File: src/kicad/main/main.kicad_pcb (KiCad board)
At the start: 2 copper layers, 38 x 75 mm, 58 parts

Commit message: Use latest faebryk features
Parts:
- removed *.mcu_pcb.co2_sensor.decoupling_caps[0][Capacitor:C], *.mcu_pcb.co2_sensor.decoupling_caps[1][Capacitor:C], *.mcu_pcb.ldo.decoupling_caps[0][Capacitor:C], *.mcu_pcb.ldo.decoupling_caps[1][Capacitor:C], *.mcu_pcb.leds.buffer.decoupling_cap[Capacitor:C], *.mcu_pcb.leds.leds[0].decoupling_cap[Capacitor:C], *.mcu_pcb.leds.leds[1].decoupling_cap[Capacitor:C], *.mcu_pcb.leds.leds[2].decoupling_cap[Capacitor:C], *.mcu_pcb.leds.leds[3].decoupling_cap[Capacitor:C], *.mcu_pcb.leds.leds[4].decoupling_cap[Capacitor:C], *.mcu_pcb.lux_sensor.decoupling_cap[Capacitor:C], *.mcu_pcb.lux_sensor.dvi_capacitor[Capacitor:C], *.mcu_pcb.mcu.debounce_capacitors[0][Capacitor:C], *.mcu_pcb.mcu.debounce_capacitors[1][Capacitor:C], *.mcu_pcb.mcu.en_rc_capacitor[Capacitor:C], *.mcu_pcb.mcu.pwr_3v3_decoupling_caps[0][Capacitor:C], *.mcu_pcb.pm_sensor.pm_sensor_buffer.buffer.decouple_caps[0][Capacitor:C], *.mcu_pcb.pm_sensor.pm_sensor_buffer.buffer.decouple_caps[1][Capacitor:C], *.mcu_pcb.usb_psu.esd_capacitor[Capacitor:C], *.mcu_pcb.usb_psu.gnd_capacitor[Capacitor:C]: C, lcsc:C0402
- removed *.mcu_pcb.co2_sensor.pullup_resistors[0][Resistor:b'10.0k\xce\xa9'], *.mcu_pcb.co2_sensor.pullup_resistors[1][Resistor:b'10.0k\xce\xa9'], *.mcu_pcb.lux_sensor.i2c_termination_resistors[0][Resistor:b'10.0k\xce\xa9'], *.mcu_pcb.lux_sensor.i2c_termination_resistors[1][Resistor:b'10.0k\xce\xa9'], *.mcu_pcb.mcu.boot_resistors[0][Resistor:b'10.0k\xce\xa9'], *.mcu_pcb.mcu.boot_resistors[1][Resistor:b'10.0k\xce\xa9'], *.mcu_pcb.mcu.debounce_resistors[0][Resistor:b'10.0k\xce\xa9'], *.mcu_pcb.mcu.debounce_resistors[1][Resistor:b'10.0k\xce\xa9'], *.mcu_pcb.mcu.en_rc_resesitor[Resistor:b'10.0k\xce\xa9']: b'10.0k\xce\xa9', lcsc:R0402
- removed *.mcu_pcb.co2_sensor.scd4x[SCD40:U]: U, lcsc:LGA-20_L10.1-W10.1-P1.25-TL
- removed *.mcu_pcb.ldo[ME6211C33M5G_N:U]: U, lcsc:SOT-23-5_L3.0-W1.7-P0.95-LS2.8-BL
- removed *.mcu_pcb.leds.buffer.buffer[pf_74AHCT2G125:U]: U, lcsc:SC-74A-5_L2.9-W1.6-P0.95-LS2.8-BR
- removed *.mcu_pcb.leds.leds[0].led[XL_3528RGBW_WS2812B:LED], *.mcu_pcb.leds.leds[1].led[XL_3528RGBW_WS2812B:LED], *.mcu_pcb.leds.leds[2].led[XL_3528RGBW_WS2812B:LED], *.mcu_pcb.leds.leds[3].led[XL_3528RGBW_WS2812B:LED], *.mcu_pcb.leds.leds[4].led[XL_3528RGBW_WS2812B:LED]: LED, lcsc:LED-SMD_4P-L3.5-W2.8-BR-1
- removed *.mcu_pcb.lux_sensor.dvi_resistor[Resistor:b'1.0k\xce\xa9'], *.mcu_pcb.pm_sensor.fan_controller.led.current_limiting_resistor[Resistor:b'1.0k\xce\xa9']: b'1.0k\xce\xa9', lcsc:R0402
- removed *.mcu_pcb.lux_sensor[BH1750FVI_TR:U]: U, lcsc:WSOF-6_L2.6-W1.6-P0.50-TL-EP
- removed *.mcu_pcb.mcu.pwr_3v3_decoupling_caps[1][Capacitor:C]: C, lcsc:C0805
- removed *.mcu_pcb.mcu.switches[0][_Switch:SW], *.mcu_pcb.mcu.switches[1][_Switch:SW]: SW, lcsc:KEY-SMD_4P-L4.2-W3.2-P2.20-LS4.6
- removed *.mcu_pcb.mcu[ESP32_C3_MINI_1_VIND:U]: U, lcsc:WIFIM-SMD_ESP32-C3-MINI-MINI-1U
- removed *.mcu_pcb.pm_sensor.fan_connector.plug[pf_533984002:J]: J, lcsc:CONN-SMD_1.25-2P
- removed *.mcu_pcb.pm_sensor.fan_controller.fan_power_switch.mosfet[MOSFET:Q]: Q, lcsc:SOT-23-3_L2.9-W1.3-P1.90-LS2.4-BR
- removed *.mcu_pcb.pm_sensor.fan_controller.fan_power_switch.pull_resistor[Resistor:b'100.0k\xce\xa9']: b'100.0k\xce\xa9', lcsc:R0402
- removed *.mcu_pcb.pm_sensor.fan_controller.flyback_protection_diode[Diode:40V]: 40V, lcsc:SOD-323_L1.8-W1.3-LS2.5-RD
- removed *.mcu_pcb.pm_sensor.fan_controller.led.led[LED:D]: D, lcsc:LED0805-RD_RED
- removed *.mcu_pcb.pm_sensor.pm_sensor_buffer.buffer[TXS0102DCUR:U]: U, lcsc:VSON8_L2.0-W2.3-P0.50-LS3.1-BL
- removed *.mcu_pcb.pm_sensor.pm_sensor_connector.plug[B4B_ZR_SM4_TF:J]: J, lcsc:CONN-SMD_ZH1.5-4AB
- removed *.mcu_pcb.pressence_sensor[HLK_LD2410B_P:U]: U, lcsc:SENSORM-TH_HLK-LD2410B-P
- removed *.mcu_pcb.qwiic_connector[QWIIC:J]: J, lcsc:CONN-SMD_BM04B-SRSS-TBT-LF-SN
- removed *.mcu_pcb.usb_psu.configuration_resistors[0][Resistor:b'5.1k\xce\xa9'], *.mcu_pcb.usb_psu.configuration_resistors[1][Resistor:b'5.1k\xce\xa9']: b'5.1k\xce\xa9', lcsc:R0402
- removed *.mcu_pcb.usb_psu.esd[USBLC6_2P6:U]: U, lcsc:SOT-666-6_L1.6-W1.2-P0.50-LS1.6-BL
- removed *.mcu_pcb.usb_psu.gnd_resistor[Resistor:b'1.0M\xce\xa9']: b'1.0M\xce\xa9', lcsc:R0402
- removed *.mcu_pcb.usb_psu.usb_connector[USB_Type_C_Receptacle_14_pin_Vertical:x]: x, lcsc:USB-C-TH_TYPE-C-USB-14P
- added C1: 100nF, lcsc:C0402, F.Cu at (1.15, 5.00)
- added C10: 100nF, lcsc:C0402, B.Cu at (0.00, 37.9)
- added C11: 100nF, lcsc:C0402, B.Cu at (0.00, 5.25)
- added C12: 1µF, lcsc:C0402, B.Cu at (-1.25, 8.75)
- added C13: 100nF, lcsc:C0402, F.Cu at (10.8, 60.0)
- added C14: 100nF, lcsc:C0402, F.Cu at (-10.8, 60.0)
- added C15: 1µF, lcsc:C0402, F.Cu at (-7.90, 22.5)
- added C16: 100nF, lcsc:C0402, F.Cu at (-15.0, 23.8)
- added C17: 10µF, lcsc:C0805, F.Cu at (-14.8, 22.0)
- added C18: 100nF, lcsc:C0402, F.Cu at (-3.00, 2.50)
- added C19: 100nF, lcsc:C0402, F.Cu at (3.00, 2.50)
- added C2: 4.7µF, lcsc:C0402, F.Cu at (1.15, 18.0)
- added C20: 1µF, lcsc:C0402, F.Cu at (-7.50, 63.5)
- added C21: 100nF, lcsc:C0402, F.Cu at (-5.50, 73.0)
- added C3: 1µF, lcsc:C0402, F.Cu at (3.00, 66.0)
- added C4: 1µF, lcsc:C0402, F.Cu at (-3.00, 66.0)
- added C5: 100nF, lcsc:C0402, F.Cu at (-1.50, 30.0)
- added C6: 100nF, lcsc:C0402, B.Cu at (0.00, 13.5)
- added C7: 100nF, lcsc:C0402, B.Cu at (0.00, 19.6)
- added C8: 100nF, lcsc:C0402, B.Cu at (0.00, 25.7)
- added C9: 100nF, lcsc:C0402, B.Cu at (0.00, 31.8)
- added D1: LED, lcsc:LED0805-RD_RED, F.Cu at (8.00, 27.5)
- added H1: Mounting_Hole, MountingHole:MountingHole_2.1mm, F.Cu at (-6.50, 2.50)
- added H2: Mounting_Hole, MountingHole:MountingHole_2.1mm, F.Cu at (7.50, 69.5)
- added H3: Mounting_Hole, MountingHole:MountingHole_2.1mm, F.Cu at (-7.50, 69.5)
- added J1: pf_533984002, lcsc:CONN-SMD_1.25-2P, F.Cu at (2.00, 23.0)
- added J2: B4B_ZR_SM4_TF, lcsc:CONN-SMD_ZH1.5-4AB, F.Cu at (13.0, 21.0)
- added J3: QWIIC, lcsc:CONN-SMD_BM04B-SRSS-TBT-LF-SN, F.Cu at (16.0, 12.5)
- added LED1: XL_3528RGBW_WS2812B, lcsc:LED-SMD_4P-L3.5-W2.8-BR-1, B.Cu at (0.00, 11.0)
- added LED2: XL_3528RGBW_WS2812B, lcsc:LED-SMD_4P-L3.5-W2.8-BR-1, B.Cu at (0.00, 17.1)
- added LED3: XL_3528RGBW_WS2812B, lcsc:LED-SMD_4P-L3.5-W2.8-BR-1, B.Cu at (0.00, 23.2)
- added LED4: XL_3528RGBW_WS2812B, lcsc:LED-SMD_4P-L3.5-W2.8-BR-1, B.Cu at (0.00, 29.3)
- added LED5: XL_3528RGBW_WS2812B, lcsc:LED-SMD_4P-L3.5-W2.8-BR-1, B.Cu at (0.00, 35.4)
- added Q1: MOSFET, lcsc:SOT-23-3_L2.9-W1.3-P1.90-LS2.4-BR, F.Cu at (2.50, 27.5)
- added R1: 10kΩ, lcsc:R0402, F.Cu at (4.25, 18.5)
- added R10: 10kΩ, lcsc:R0402, F.Cu at (-9.40, 22.5)
- added R11: 100kΩ, lcsc:R0402, F.Cu at (2.50, 30.0)
- added R12: 1kΩ, lcsc:R0402, F.Cu at (8.00, 30.5)
- added R13: 390Ω, lcsc:R0402, F.Cu at (5.00, 1.75)
- added R14: 390Ω, lcsc:R0402, F.Cu at (5.00, 3.00)
- added R15: 5.1kΩ, lcsc:R0402, F.Cu at (2.50, 68.5)
- added R16: 5.1kΩ, lcsc:R0402, F.Cu at (-2.50, 68.5)
- added R17: 1MΩ, lcsc:R0402, F.Cu at (5.50, 73.0)
- added R2: 10kΩ, lcsc:R0402, F.Cu at (5.50, 18.5)
- added R3: 1kΩ, lcsc:R0402, B.Cu at (1.25, 8.75)
- added R4: 10kΩ, lcsc:R0402, B.Cu at (-12.2, 12.0)
- added R5: 10kΩ, lcsc:R0402, B.Cu at (-12.2, 13.2)
- added R6: 10kΩ, lcsc:R0402, F.Cu at (-4.25, 10.2)
- added R7: 10kΩ, lcsc:R0402, F.Cu at (-11.8, 22.5)
- added R8: 10kΩ, lcsc:R0402, F.Cu at (10.8, 63.0)
- added R9: 10kΩ, lcsc:R0402, F.Cu at (-10.8, 63.0)
- added SW1: _Switch, lcsc:KEY-SMD_4P-L4.2-W3.2-P2.20-LS4.6, F.Cu at (13.5, 61.5)
- added SW2: _Switch, lcsc:KEY-SMD_4P-L4.2-W3.2-P2.20-LS4.6, F.Cu at (-13.5, 61.5)
- added U1: SCD40, lcsc:LGA-20_L10.1-W10.1-P1.25-TL, F.Cu at (3.00, 11.5)
- added U2: ME6211C33M5G_N, lcsc:SOT-23-5_L3.0-W1.7-P0.95-LS2.8-BL, F.Cu at (0.00, 66.0)
- added U3: pf_74AHCT2G125, lcsc:SC-74A-5_L2.9-W1.6-P0.95-LS2.8-BR, F.Cu at (-1.50, 27.5)
- added U4: BH1750FVI_TR, lcsc:WSOF-6_L2.6-W1.6-P0.50-TL-EP, B.Cu at (0.00, 7.00)
- added U5: ESP32_C3_MINI_1_VIND, lcsc:WIFIM-SMD_ESP32-C3-MINI-MINI-1U, F.Cu at (-11.0, 13.0)
- added U6: TXS0102DCUR, lcsc:VSON8_L2.0-W2.3-P0.50-LS3.1-BL, F.Cu at (0.00, 2.50)
- added U7: HLK_LD2410B_P, lcsc:SENSORM-TH_HLK-LD2410B-P, B.Cu at (16.2, 61.5)
- added U8: USBLC6_2P6, lcsc:SOT-666-6_L1.6-W1.2-P0.50-LS1.6-BL, F.Cu at (-5.00, 64.5)
- added x1: USB_Type_C_Receptacle_14_pin_Vertical, lcsc:USB-C-TH_TYPE-C-USB-14P, F.Cu at (0.00, 73.2)
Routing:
- added copper zone on B.Cu, net GND
- added copper zone on F.Cu, net GND
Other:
- outline, holes or cut-outs redrawn
- copper layers 2 -> 4

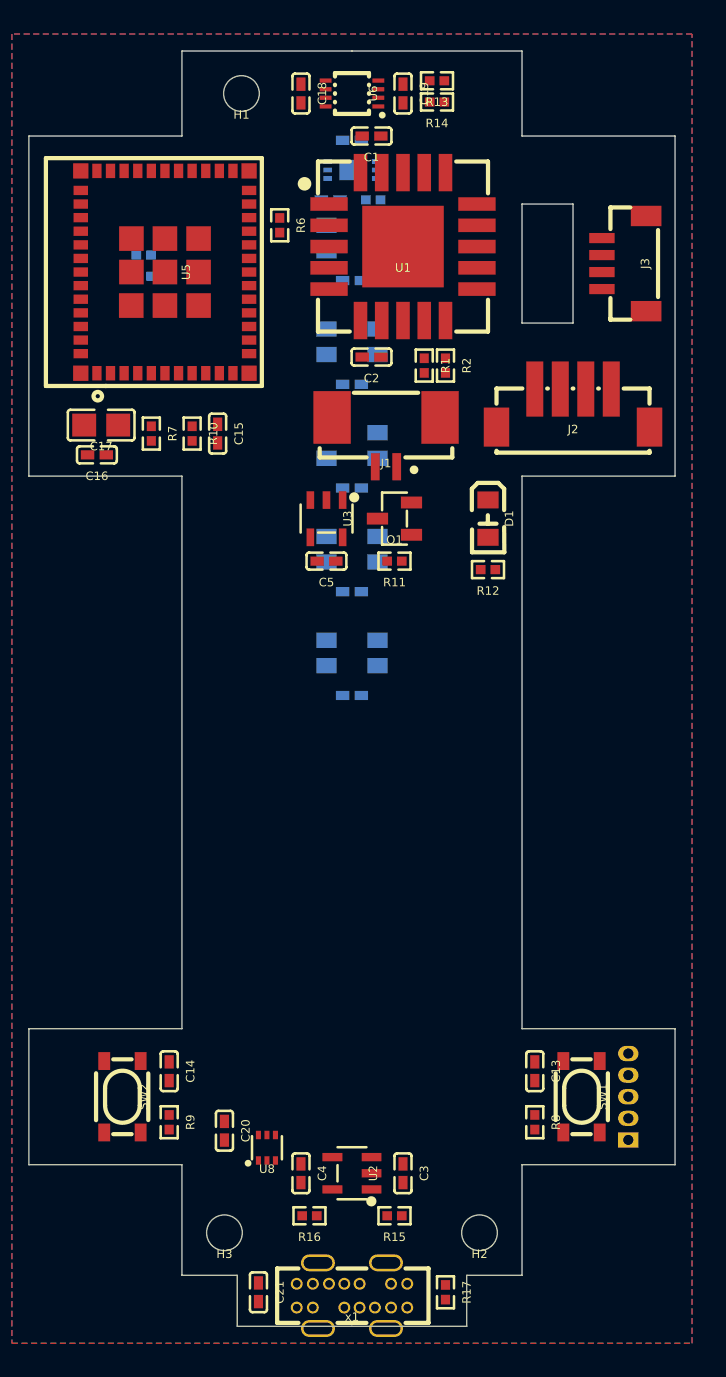
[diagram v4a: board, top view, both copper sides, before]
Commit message: Partial routing
Fix coordinate typo
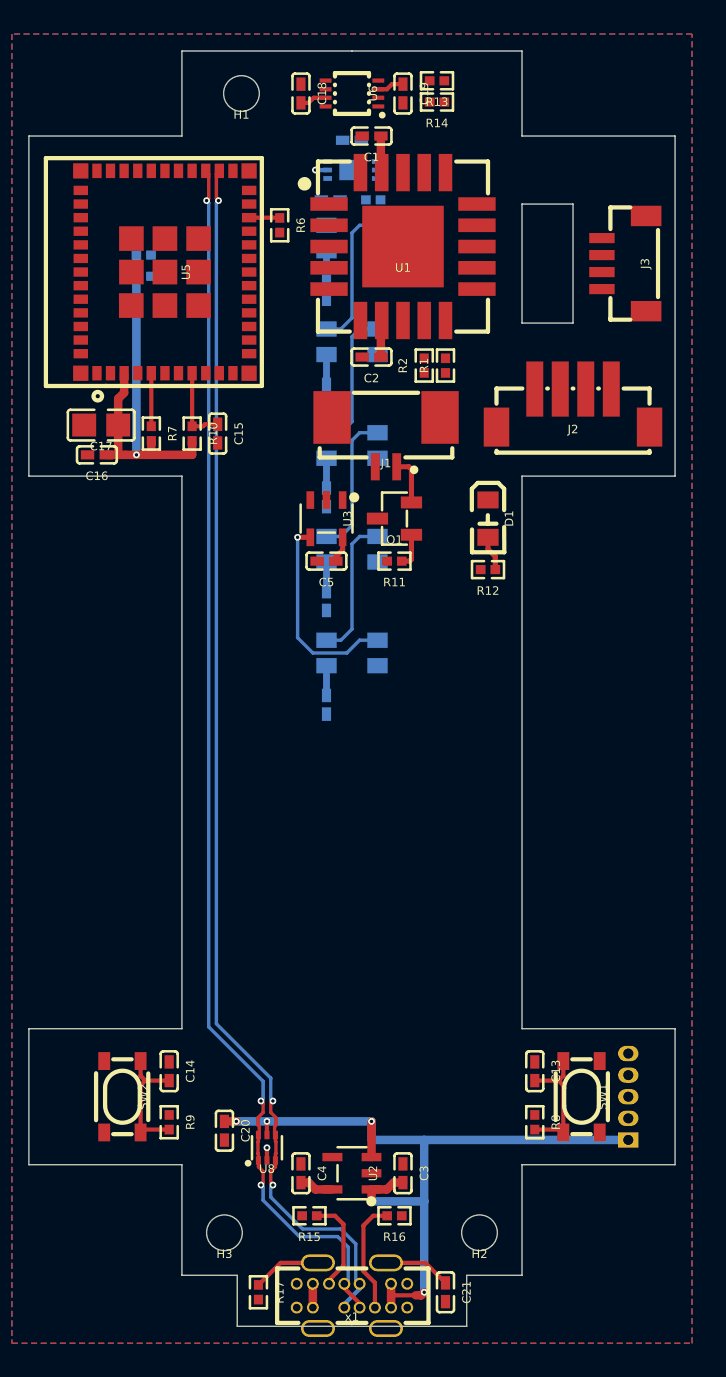
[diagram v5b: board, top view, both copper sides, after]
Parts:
- moved C6 25.0 mm to (-1.50, 38.4), turned to -90 degrees
- moved LED1 24.4 mm to (0.00, 35.4)
- moved LED5 24.4 mm to (0.00, 11.0)
- moved C10 23.9 mm to (-1.50, 14.1), turned to -90 degrees
- moved C7 12.8 mm to (-1.50, 32.4), turned to -90 degrees
- moved LED2 12.2 mm to (0.00, 29.3)
- moved LED4 12.2 mm to (0.00, 17.1)
- moved C9 11.7 mm to (-1.50, 20.2), turned to -90 degrees
- moved C21 11.0 mm to (5.50, 73.0), turned to 270 degrees
- moved R17 11.0 mm to (-5.50, 73.0), turned to 270 degrees
- moved R15 5.00 mm to (-2.50, 68.5)
- moved R16 5.00 mm to (2.50, 68.5)
- moved C8 1.60 mm to (-1.50, 26.2), turned to -90 degrees
- moved R1 1.25 mm to (5.50, 18.5), turned to -90 degrees
- moved R2 1.25 mm to (4.25, 18.5), turned to -90 degrees
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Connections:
- net J3-3-R1-1-R4-1-U1-10-U4-4-U5-19 renamed SDA
- net J3-4-R2-1-R5-1-U1-9-U4-6-U5-18 renamed SCL
- net U5-12-U7-3 renamed U0_RX
- net U5-13-U7-2 renamed U0_TX
- net U5-26-U8-3-U8-4-x1-10-x1-3 renamed USB_DN
- net U5-27-U8-1-U8-6-x1-11-x1-4 renamed USB_DP
- C1 pad 1: C1-1-C2-1-U1-19-U1-7 -> 3V3
- C1 pad 2: C1-2-C2-2-U1-20-U1-21-U1-6 -> GND
- C15 pad 1: C15-1-R10-1-R8-1-R9-1-U5-8 -> C15-1-R10-1-R9-1-U5-8
- C18 pad 1: C18-1-C19-1-U6-3-U6-7 -> 3V3
- C18 pad 2: C18-2-C19-2-U6-2-U6-6 -> GND
- C19 pad 1: C18-1-C19-1-U6-3-U6-7 -> 3V3
- C19 pad 2: C18-2-C19-2-U6-2-U6-6 -> GND
- C2 pad 1: C1-1-C2-1-U1-19-U1-7 -> 3V3
- C2 pad 2: C1-2-C2-2-U1-20-U1-21-U1-6 -> GND
- D1 pad 1: D1-1 -> VBUS
- J2 pad 1: J2-1 -> J2-1-R14-2
- J2 pad 2: J2-2 -> J2-2-R13-2
- R10 pad 1: C15-1-R10-1-R8-1-R9-1-U5-8 -> C15-1-R10-1-R9-1-U5-8
- R13 pad 1: R13-1 -> U1_RX_BHV
- R13 pad 2: R13-2 -> J2-2-R13-2
- R14 pad 1: R14-1 -> U1_TX_BHV
- R14 pad 2: R14-2 -> J2-1-R14-2
- R8 pad 1: C15-1-R10-1-R8-1-R9-1-U5-8 -> R8-1-U5-23
- R9 pad 1: C15-1-R10-1-R8-1-R9-1-U5-8 -> C15-1-R10-1-R9-1-U5-8
- U1 pad 19: C1-1-C2-1-U1-19-U1-7 -> 3V3
- U1 pad 20: C1-2-C2-2-U1-20-U1-21-U1-6 -> GND
- U1 pad 21: C1-2-C2-2-U1-20-U1-21-U1-6 -> GND
- U1 pad 6: C1-2-C2-2-U1-20-U1-21-U1-6 -> GND
- U1 pad 7: C1-1-C2-1-U1-19-U1-7 -> 3V3
- U5 pad 23: U5-23 -> R8-1-U5-23
- U5 pad 30: U5-30 -> U1_RX
- U5 pad 31: U5-31 -> U1_TX
- U5 pad 8: C15-1-R10-1-R8-1-R9-1-U5-8 -> C15-1-R10-1-R9-1-U5-8
- U6 pad 1: U6-1 -> U1_RX_BHV
- U6 pad 2: C18-2-C19-2-U6-2-U6-6 -> GND
- U6 pad 3: C18-1-C19-1-U6-3-U6-7 -> 3V3
- U6 pad 4: U6-4 -> U1_RX
- U6 pad 5: U6-5 -> U1_TX
- U6 pad 6: C18-2-C19-2-U6-2-U6-6 -> GND
- U6 pad 7: C18-1-C19-1-U6-3-U6-7 -> 3V3
- U6 pad 8: U6-8 -> U1_TX_BHV
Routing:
- net USB_DP: track 0.00 -> 72.7 mm, vias 0 -> 3
- net USB_DN: track 0.00 -> 72.7 mm, vias 0 -> 3
- net VBUS: track 0.00 -> 56.0 mm, vias 0 -> 5
- net 3V3: track 0.00 -> 32.9 mm, vias 0 -> 1
- net LED1-1-U3-4: track 0.00 -> 12.0 mm, vias 0 -> 1
- net LED4-4-LED5-1: track 0.00 -> 8.46 mm
- net LED2-4-LED3-1: track 0.00 -> 8.46 mm
- net LED1-4-LED2-1: track 0.00 -> 8.46 mm
- net LED3-4-LED4-1: track 0.00 -> 8.46 mm
- net C21-1-R17-1-x1-0: track 0.00 -> 8.03 mm
- net C14-1-R9-2-SW2-1-SW2-2: track 0.00 -> 7.58 mm
- net C13-1-R8-2-SW1-1-SW1-2: track 0.00 -> 7.58 mm
- net R16-1-x1-5: track 0.00 -> 6.74 mm
- net R15-1-x1-12: track 0.00 -> 5.63 mm
- net C15-1-R10-1-R9-1-U5-8: track 0.00 -> 4.67 mm
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- added copper zone on In1.Cu, net GND
- added copper zone on In2.Cu, net GND
